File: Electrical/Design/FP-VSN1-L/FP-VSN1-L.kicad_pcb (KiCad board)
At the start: 2 copper layers, 105.6 x 105.6 mm, 17 parts

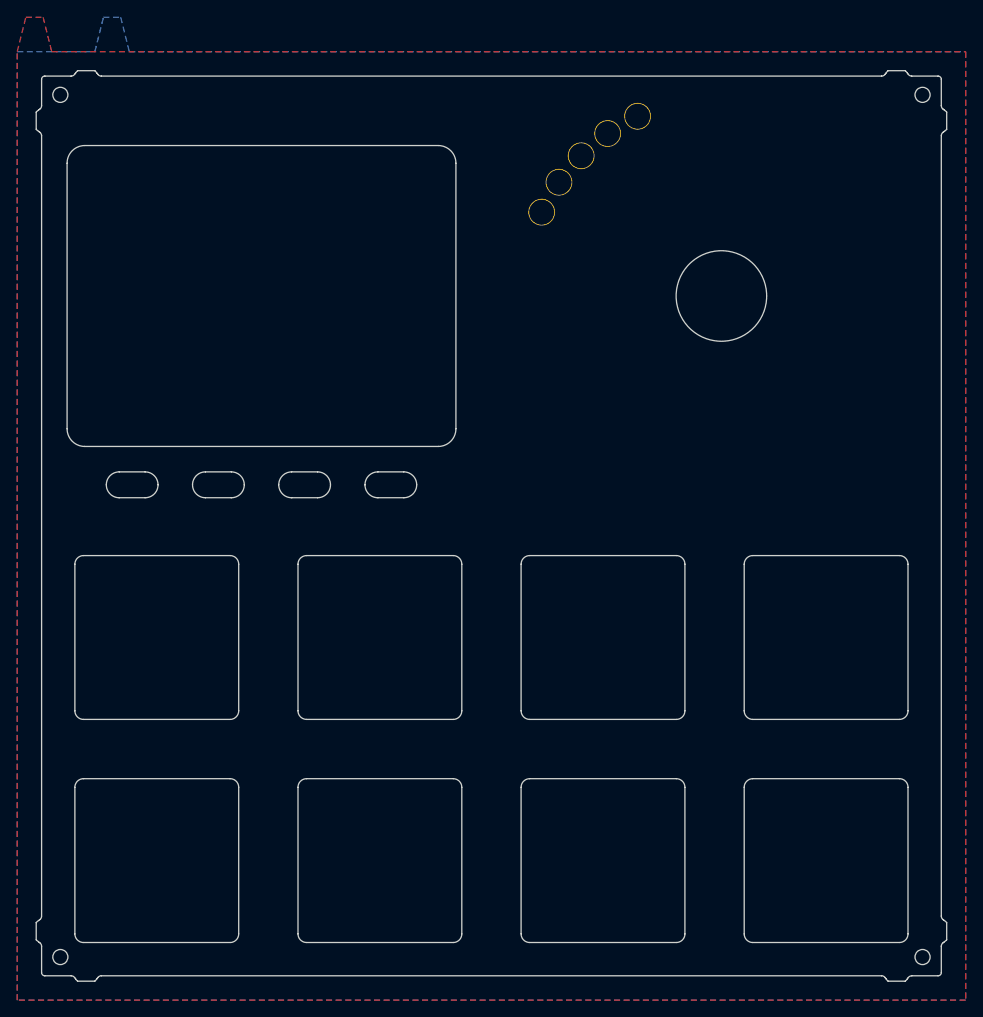
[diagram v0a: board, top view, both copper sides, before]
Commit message: outline change + VSN window size change
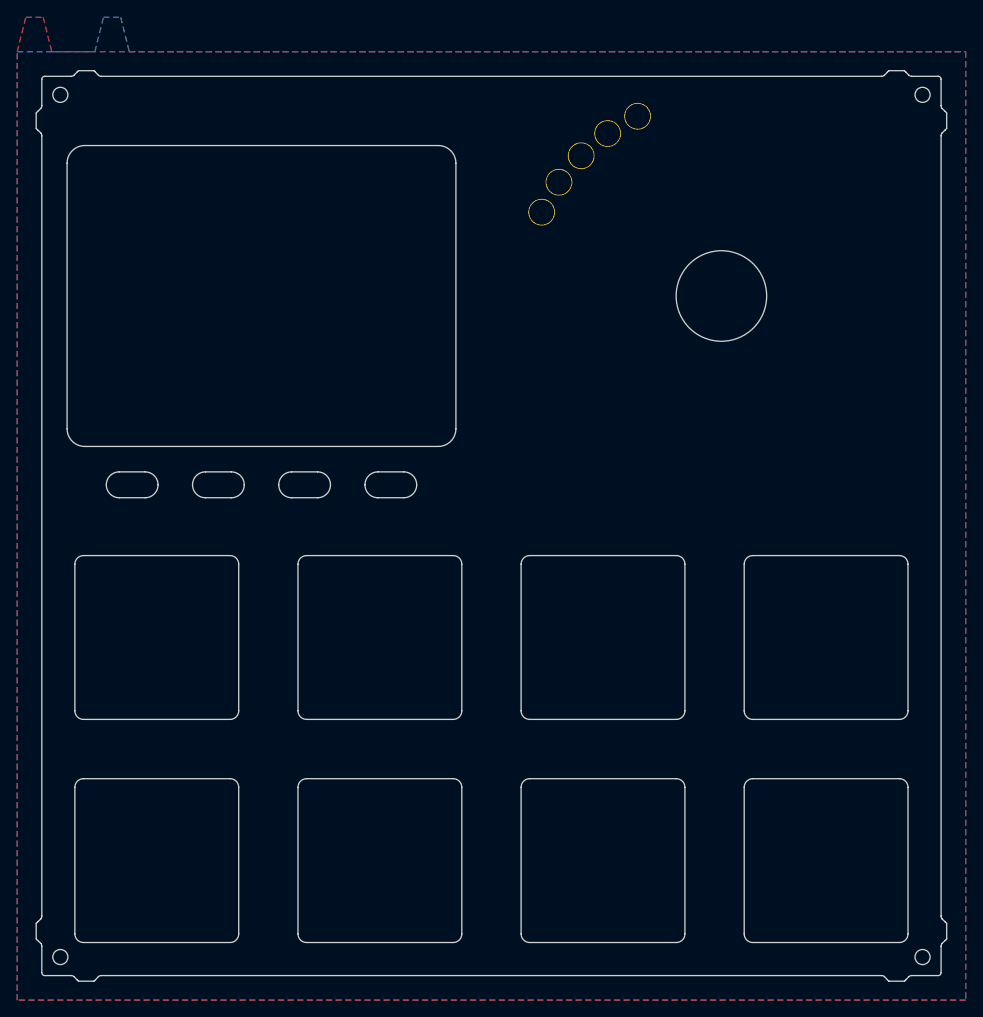
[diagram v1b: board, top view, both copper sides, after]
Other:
- outline, holes or cut-outs redrawn
